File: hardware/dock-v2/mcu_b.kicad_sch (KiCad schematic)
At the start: 31 parts, among them SW401 SW_Push, U401 RP2354A, Y401 12MHz

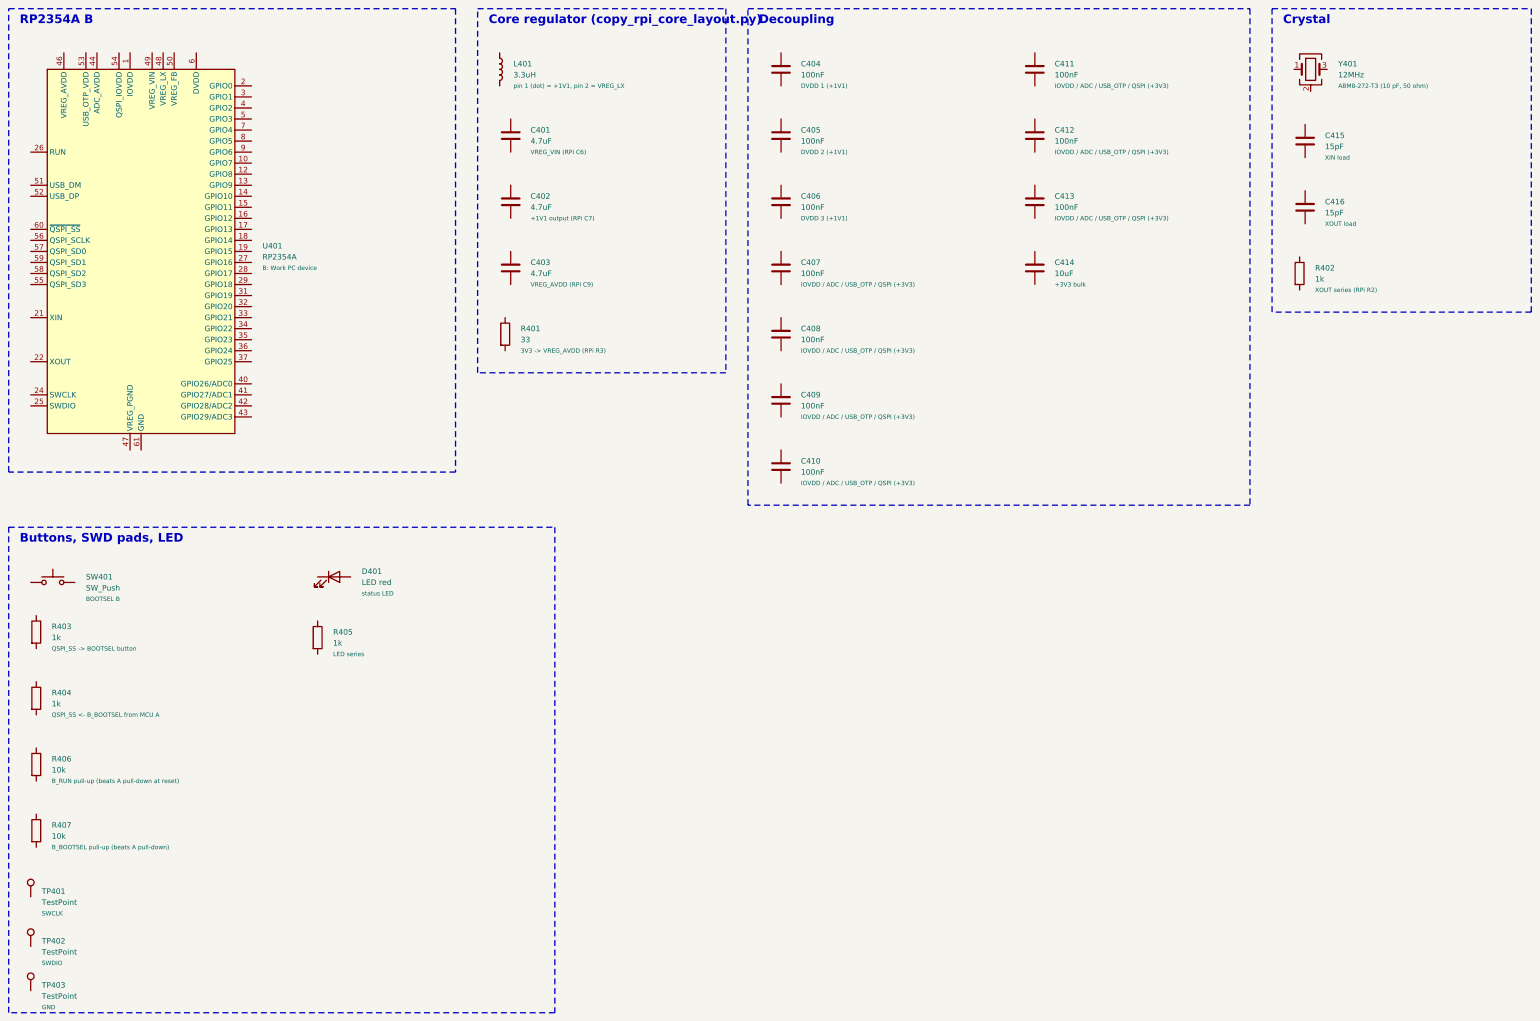
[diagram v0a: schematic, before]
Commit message: Dock v2 schematic: wiring in progress (user's work, snapshot before fixes)
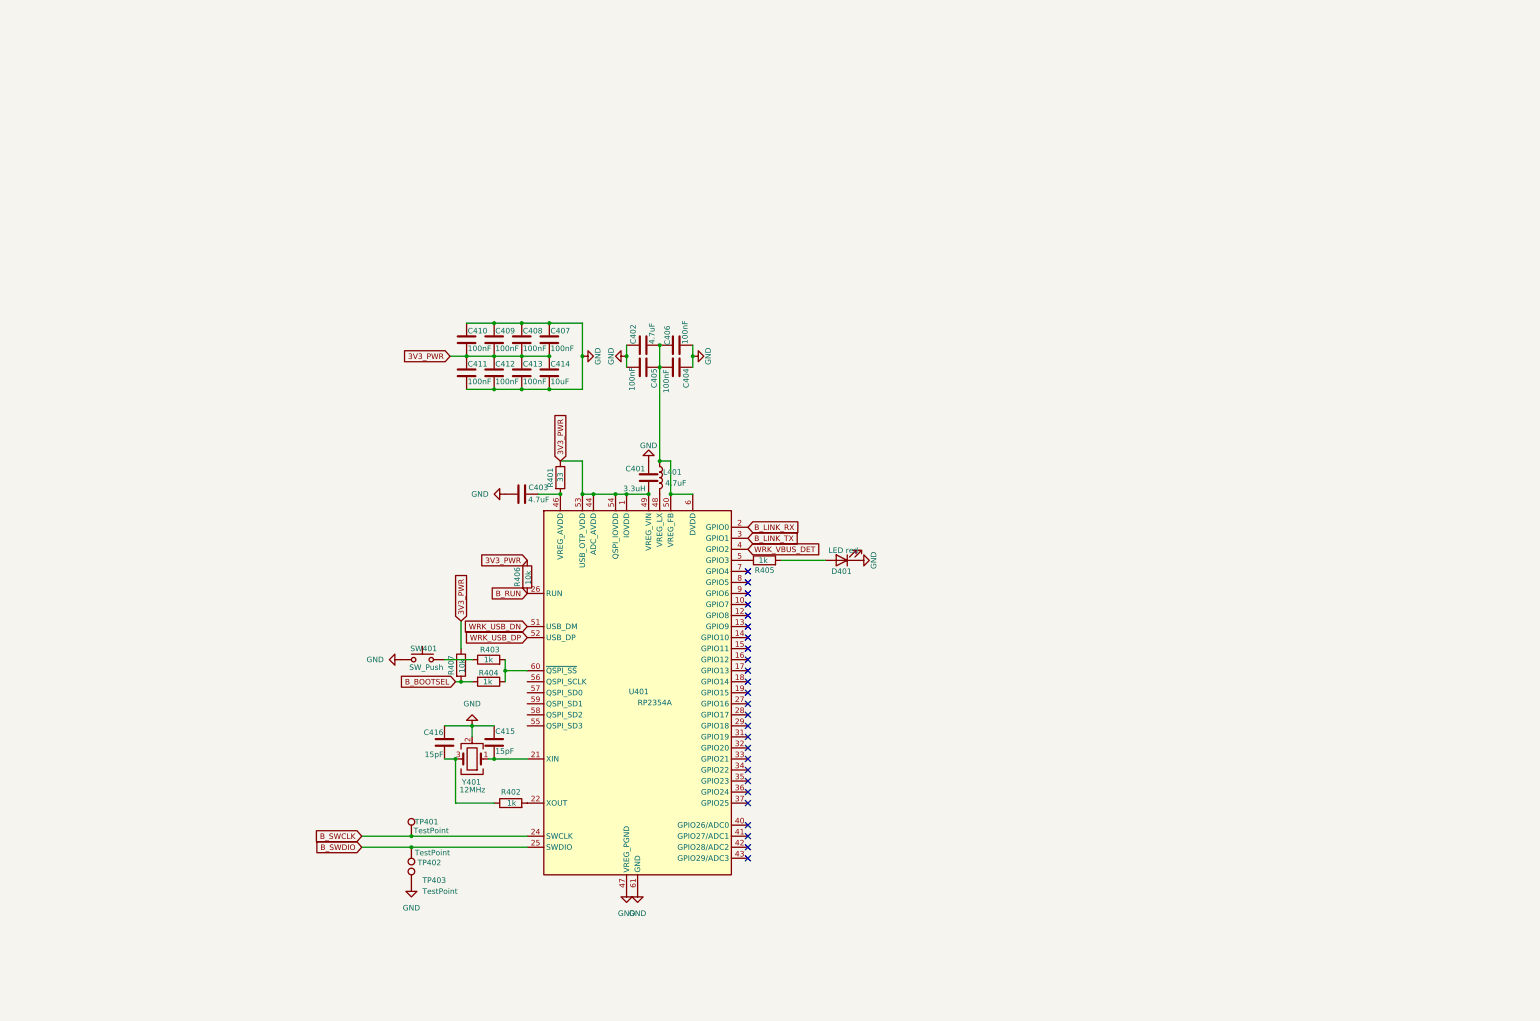
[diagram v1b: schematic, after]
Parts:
- R406: LCSC C25744 -> C11702; Note B_RUN pull-up (beats A pull-down at reset) -> LED series
- R407: LCSC C25744 -> C11702; Note B_BOOTSEL pull-up (beats A pull-down) -> LED series
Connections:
- net at L401.1: now also C402.2, C404.2, C405.1, C406.1, U401.23 (DVDD), U401.39 (DVDD), U401.50 (VREG_FB), U401.6 (DVDD)
- net at L401.2: now also U401.48 (VREG_LX)
- net 3V3_PWR: now reaches C412.1
- net 3V3_PWR: now also C401.2, C407.2, C408.2, C409.2, C410.2, C411.1, C413.1, C414.1, R401.1, R406.1, R407.1, U401.1 (IOVDD), U401.11 (IOVDD), U401.20 (IOVDD), U401.30 (IOVDD), U401.38 (IOVDD), U401.44 (ADC_AVDD), U401.45 (IOVDD), U401.49 (VREG_VIN), U401.53 (USB_OTP_VDD), U401.54 (QSPI_IOVDD)
- net GND: now reaches C412.2
- net GND: now also C401.1, C402.1, C403.1, C404.1, C405.2, C406.2, C407.1, C408.1, C409.1, C410.1, C411.2, C413.2, C414.2, C415.1, C416.2, D401.1 (K), SW401.1, TP403.1, U401.47 (VREG_PGND), U401.61 (GND), Y401.2 (G), Y401.4 (G)
- net B_BOOTSEL: now reaches R407.2
- net B_BOOTSEL: now also R404.2
- net at R405.1: now also U401.5 (GPIO3)
- net at R405.2: now also D401.2 (A)
- net at SW401.2: now also R403.1
- net at C416.1: now also R402.1, Y401.3
- net at R402.2: now also U401.22 (XOUT)
- net B_RUN: now reaches R406.2
- net B_RUN: now also U401.26 (RUN)
- net at C415.2: now also U401.21 (XIN), Y401.1
- net at R404.1: now also R403.2, U401.60 (~{QSPI_SS})
- net at C403.2: now also R401.2, U401.46 (VREG_AVDD)
- net B_LINK_RX: now reaches U401.2 (GPIO0)
- net B_SWCLK: now reaches U401.24 (SWCLK)
- net B_SWCLK: now also TP401.1
- net B_SWDIO: now reaches U401.25 (SWDIO)
- net B_SWDIO: now also TP402.1
- net B_LINK_TX: now reaches U401.3 (GPIO1)
- net WRK_VBUS_DET: now reaches U401.4 (GPIO2)
- net WRK_USB_DN: now reaches U401.51 (USB_DM)
- net WRK_USB_DP: now reaches U401.52 (USB_DP)
- no-connect marks 0 -> 26
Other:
- note removed: "Buttons, SWD pads, LED"
- note removed: "Core regulator (copy_rpi_core_layout.py)"
- note removed: "Crystal"
- note removed: "Decoupling"
- note removed: "RP2354A B"
